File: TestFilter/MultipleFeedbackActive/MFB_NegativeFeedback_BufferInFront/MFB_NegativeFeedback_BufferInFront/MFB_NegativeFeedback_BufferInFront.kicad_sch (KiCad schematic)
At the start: 9 parts, among them U1 ${SIM.PARAMS}, U2 ${SIM.PARAMS}

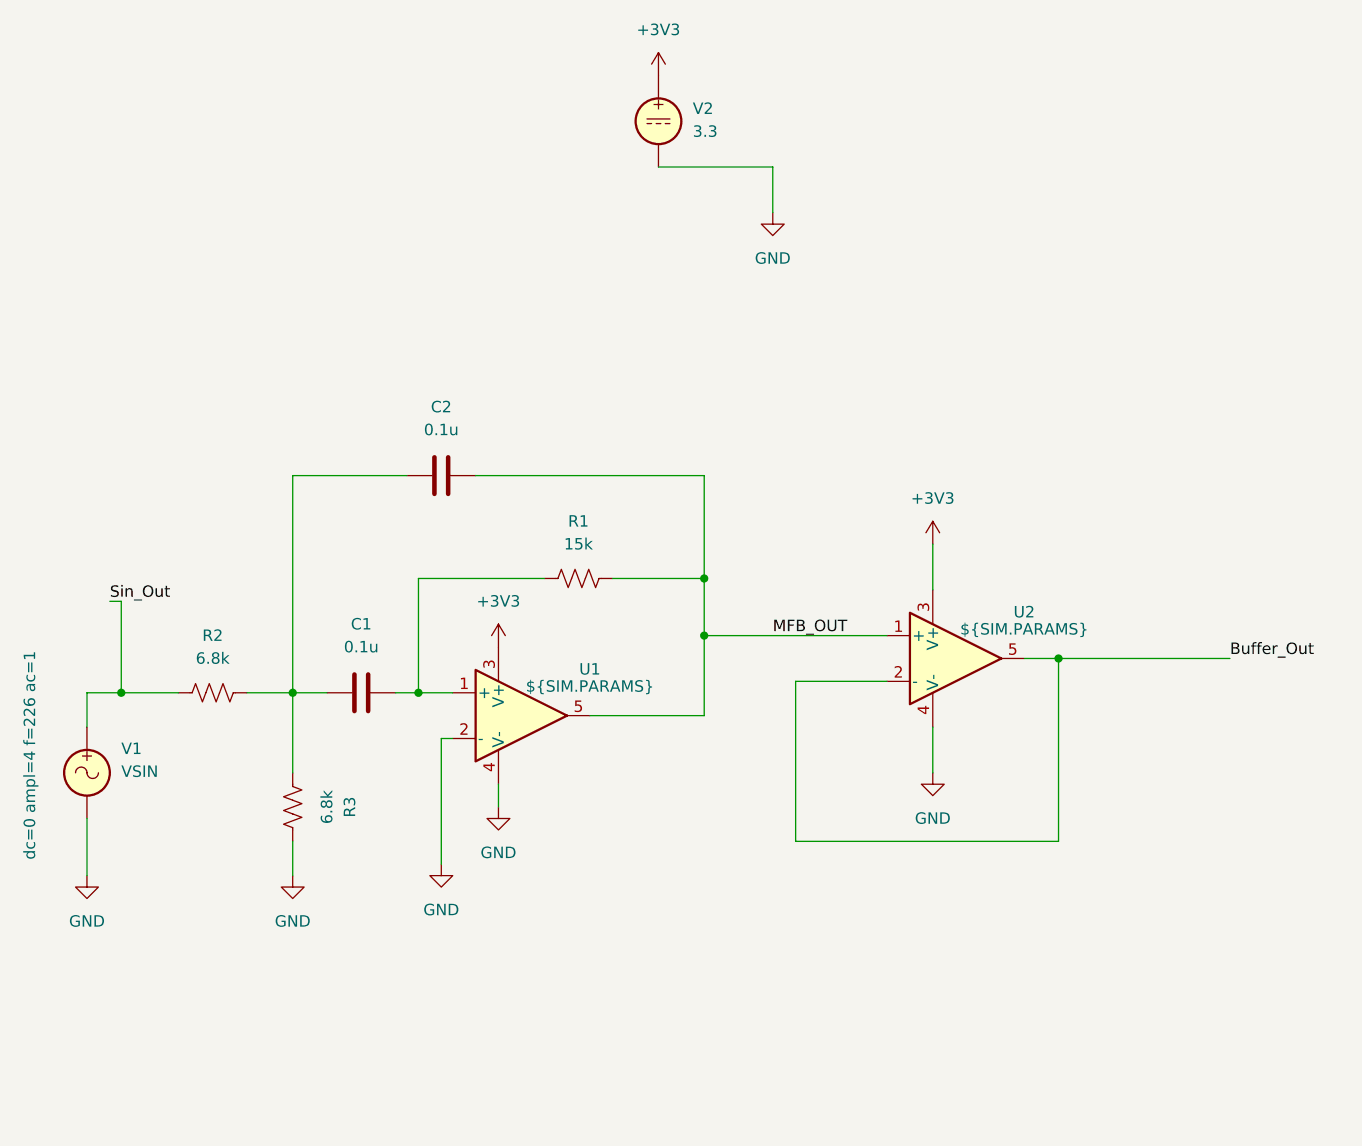
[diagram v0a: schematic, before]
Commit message: update MultipleFeedbackActive schematic; add MFB_NegativeFeedback_BufferInFront variant
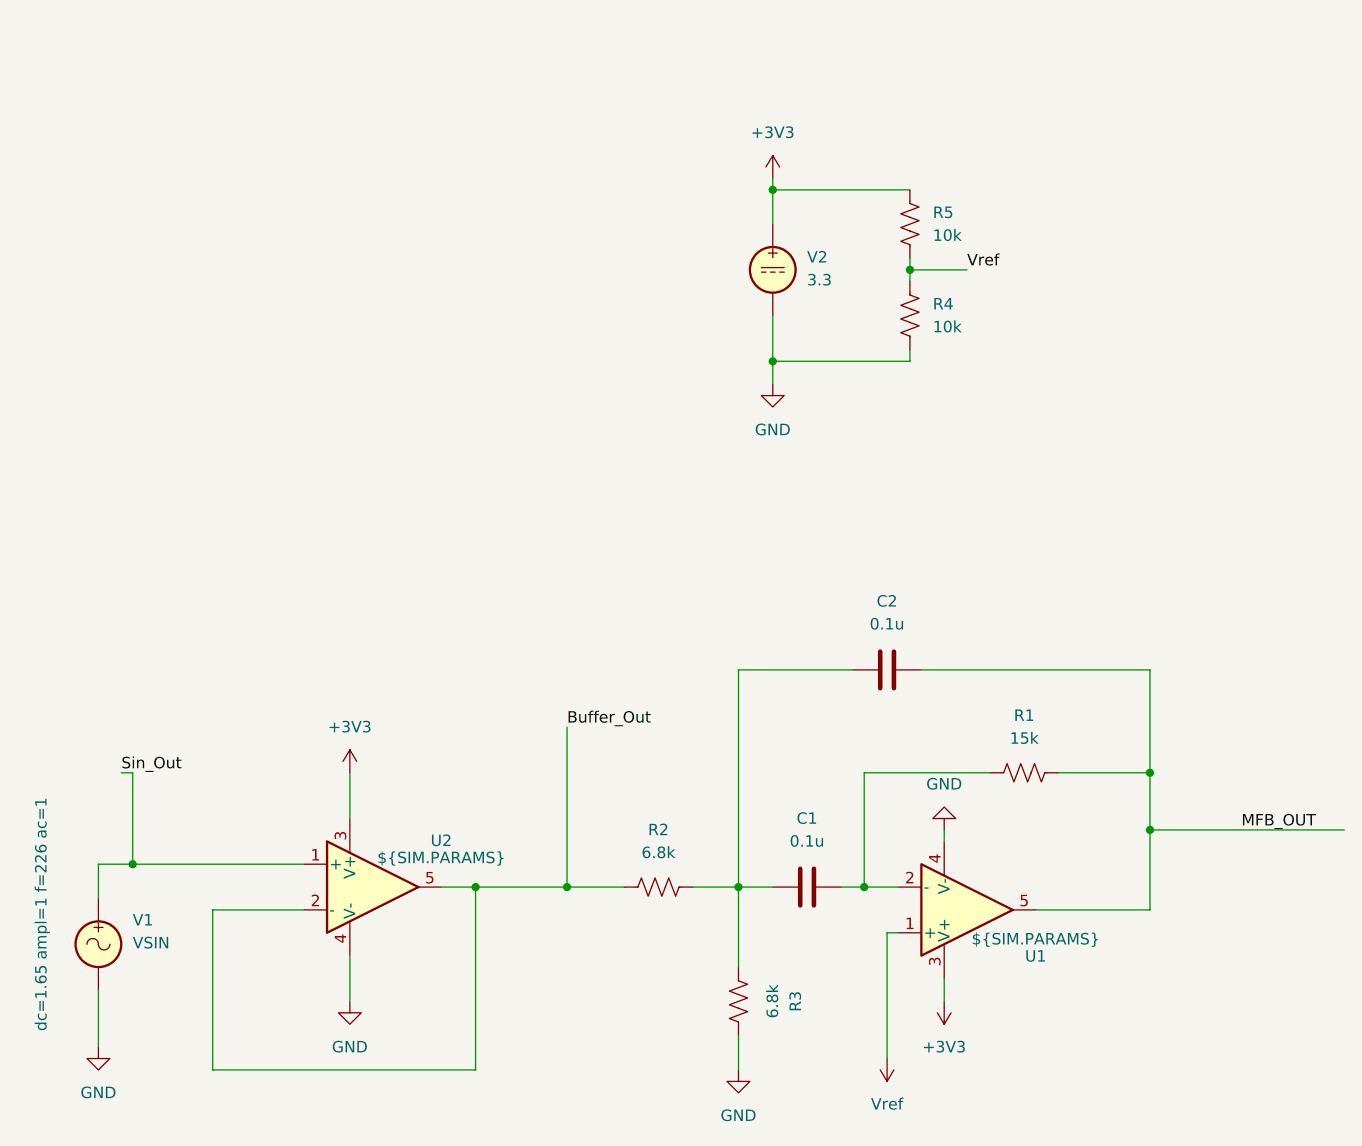
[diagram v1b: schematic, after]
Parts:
- added R4, R5: 10k, symbol Device:R_US
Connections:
- net +3V3: now also R5.1
- net Buffer_Out: now also R2.1
- net GND: now also R4.2; no longer U1.2 (-)
- net MFB_OUT: no longer U2.1 (+)
- net Sin_Out: now also U2.1 (+); no longer R2.1
- net at C1.2, R1.1: now also U1.2 (-); no longer U1.1 (+)
- new net Vref: R4.1, R5.2, U1.1 (+)
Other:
- moved on the sheet: C1, C2, R1, R2, R3, U1, U2, V1, V2
